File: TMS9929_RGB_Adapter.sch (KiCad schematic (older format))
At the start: 59 parts, among them P1 CONN_01X06, P10 12V, P2 CONN_01X08, P3 SEL, P4 SEL, P5 SEL, P6 CONN_01X01, P7 CONN_01X01, P8 CONN_01X01, P9 CONN_01X01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

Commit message: Initial changes to new version, copyright, DRC, etc.
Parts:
- U6: symbol TL071 -> TL071-RESCUE-TMS9929_RGB_Adapter
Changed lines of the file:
@@
 EESchema Schematic File Version 2
+LIBS:TMS9929_RGB_Adapter-rescue
 LIBS:power
 LIBS:device
@@
 Sheet 1 1
 Title "TMS9929A to RGB"
-Date "2016-06-20"
+Date "2017-09-17"
 Rev "0"
-Comp "Alexis Kotlowy"
-Comment1 ""
+Comp "Gerhard Wiesinger"
+Comment1 "Based on Alexis Kotlowy"
 Comment2 ""
 Comment3 ""
@@
 U
 $Comp
-L TL071 U6
+L TL071-RESCUE-TMS9929_RGB_Adapter U6
 U 1 1 57686080
 P 10650 4850

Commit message: Updated schematic & PCB for added Cinch connectors as well as power supply connector and damping resistors/jumpers
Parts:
- added JDC1: Jack-DC, jack_2mm:jack_2mm, symbol Jack-DC
- added JUIN1, JUOUT1: Conn_01x02, rca_white, symbol Conn_01x02
- added JUSHORT1, JVSHORT1, JYINSHORT1: Conn_01x02, Pin_Header_Straight_1x02_Pitch2.54mm, symbol Conn_01x02
- added JVIN1, JVOUT1: Conn_01x02, rca_red, symbol Conn_01x02
- added JYIN1, JYOUT1: Conn_01x02, rca_black, symbol Conn_01x02
- added RUIN1, RVIN1, RYIN1: 10E, Resistors_SMD:R_0805_HandSoldering, symbol R
- added RYIN2: 10k, Resistors_SMD:R_0805_HandSoldering, symbol R
- P1: footprint Pin_Headers:Pin_Header_Straight_1x06 -> Pin_Headers:Pin_Header_Straight_1x06_Pitch2.54mm
- P2: footprint Pin_Headers:Pin_Header_Straight_1x08 -> Pin_Headers:Pin_Header_Straight_1x08_Pitch2.54mm
- P3, P4, P5: footprint Pin_Headers:Pin_Header_Straight_1x03 -> Pin_Headers:Pin_Header_Straight_1x03_Pitch2.54mm
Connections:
- net GND: now also JDC1.2, JDC1.3, JUIN1.1 (Pin_1), JUOUT1.1 (Pin_1), JVIN1.1 (Pin_1), JVOUT1.1 (Pin_1), JYIN1.1 (Pin_1), JYOUT1.1 (Pin_1)
- net U: now also JUIN1.2 (Pin_2)
- net VCC: now also JDC1.1
- net Vref: now also RYIN2.1
- net at R28.2, U2.3 (+): now also JVSHORT1.2 (Pin_2), RVIN1.2; no longer U4.3 (O/I)
- net at R29.2, U3.3 (+): now also JUSHORT1.2 (Pin_2), RUIN1.2; no longer U4.9 (O/I)
- net YIN: now reaches C6.1, P1.3 (P3)
- net YIN: now also JYIN1.2 (Pin_2), JYINSHORT1.1 (Pin_1), RYIN1.1; no longer U1.3 (+)
- net at C3.2, P2.5 (P5): now also JUOUT1.2 (Pin_2)
- net at C2.2, P2.4 (P4): now also JVOUT1.2 (Pin_2)
- net at C1.2, P2.3 (P3): now also JYOUT1.2 (Pin_2)
- net V: now reaches P1.5 (P5), U4.4 (I/O)
- net V: now also JVIN1.2 (Pin_2)
- new net: JYINSHORT1.2 (Pin_2), RYIN1.2, RYIN2.2, U1.3 (+)
- new net: JUSHORT1.1 (Pin_1), RUIN1.1, U4.9 (O/I)
- new net: JVSHORT1.1 (Pin_1), RVIN1.1, U4.3 (O/I)
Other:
- moved on the sheet: P10, R28, R29

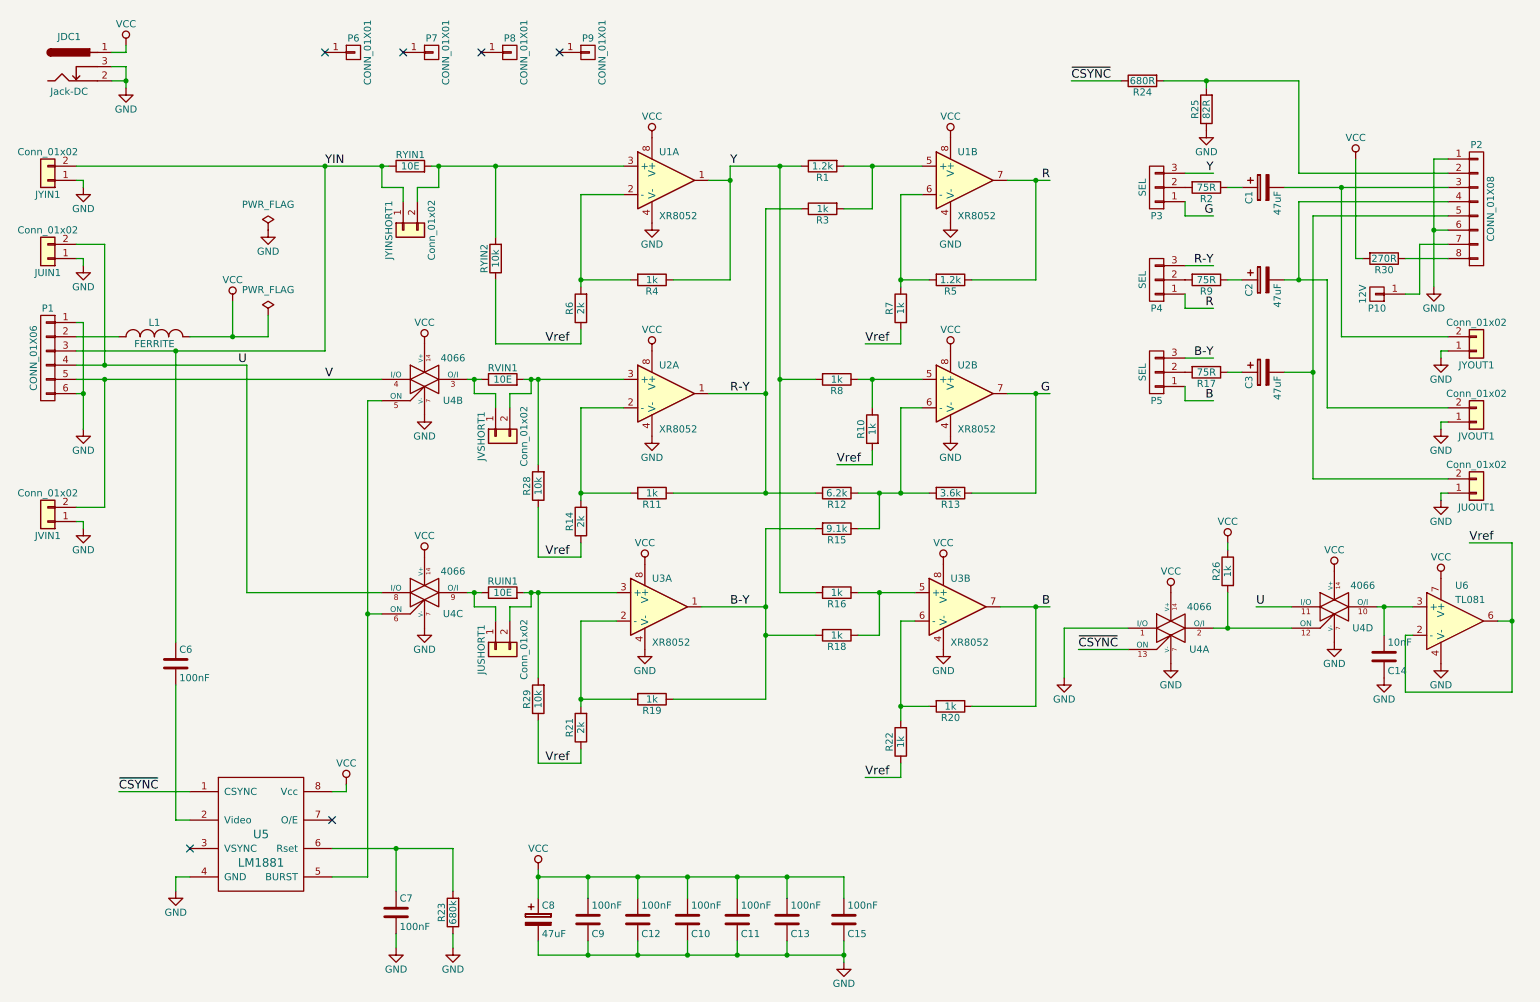
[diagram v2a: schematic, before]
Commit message: schematic: Added comments for power supply, moved capacitor at TL081 (cosmetics)
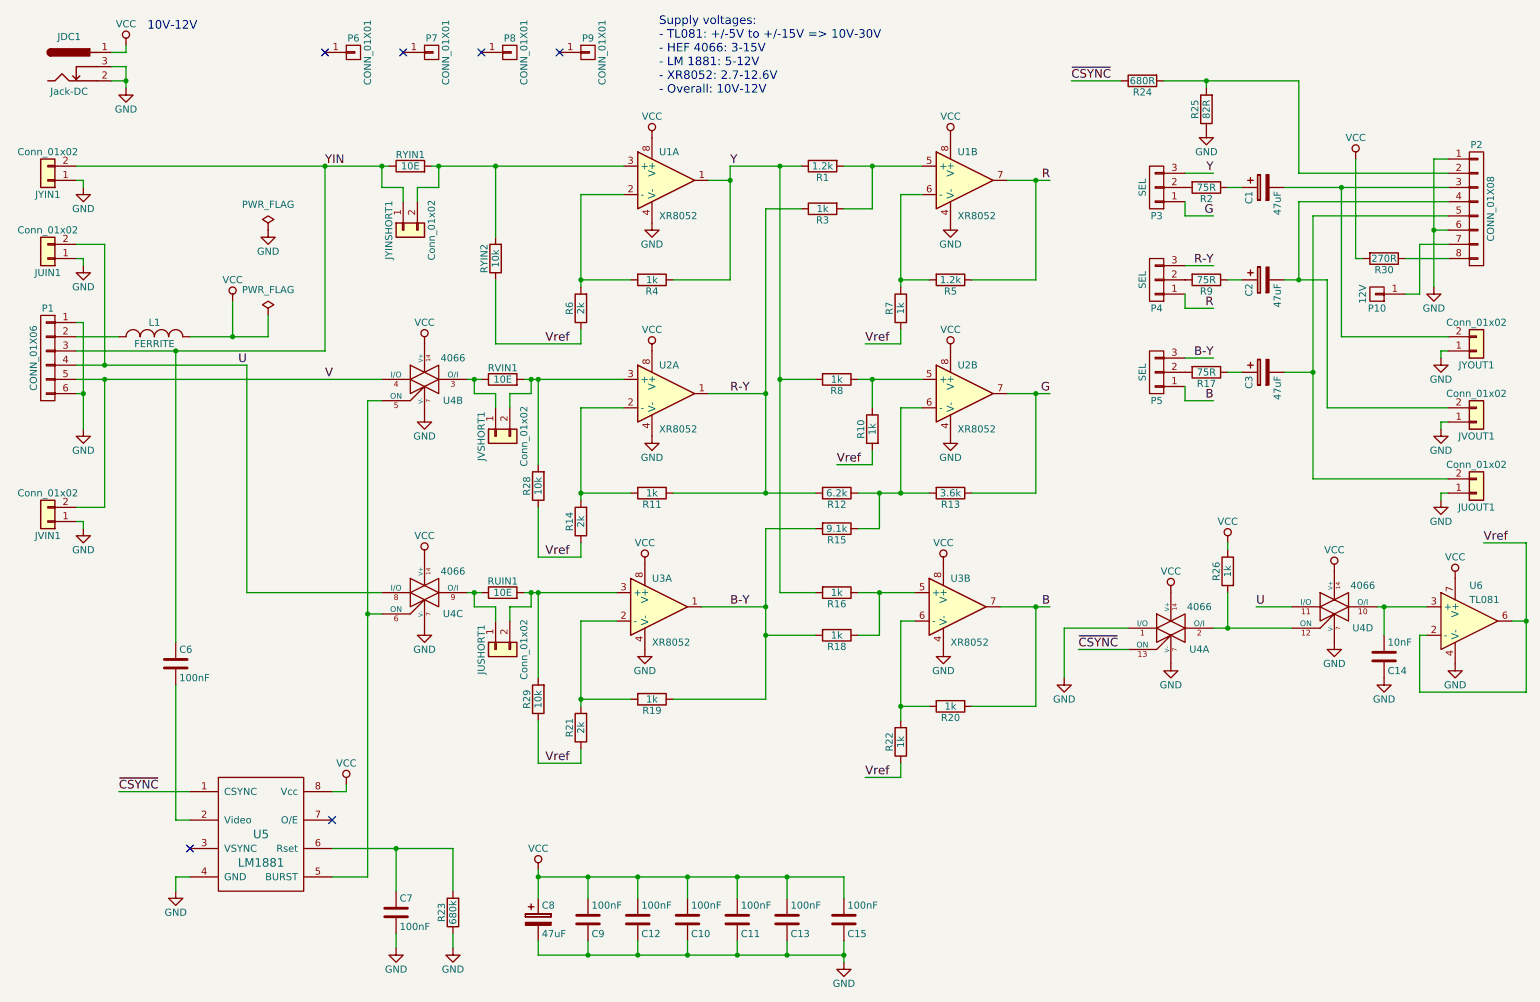
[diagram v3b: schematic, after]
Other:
- note added: "10V-12V"
- note added: "Supply voltages:\n- TL081: +/-5V to +/-15V => 10V-30V\n- HEF 4066: 3-15V\n- LM 1881: 5-12V\n- XR8052: 2.7-12.6V\n- Overall: 10V-12V\n"
- moved on the sheet: U6
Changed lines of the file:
@@
 L TL071-RESCUE-TMS9929_RGB_Adapter U6
 U 1 1 57686080
-P 10650 4850
-F 0 "U6" H 10650 5100 50  0000 L CNN
-F 1 "TL081" H 10650 5000 50  0000 L CNN
-F 2 "SMD_Packages:SOIC-8-N" H 10700 5050 50  0001 C CNN
-F 3 "" H 10650 5100 50  0000 C CNN
-	1    10650 4850
+P 10750 4850
+F 0 "U6" H 10750 5100 50  0000 L CNN
+F 1 "TL081" H 10750 5000 50  0000 L CNN
+F 2 "SMD_Packages:SOIC-8-N" H 10800 5050 50  0001 C CNN
+F 3 "" H 10750 5100 50  0000 C CNN
+	1    10750 4850
 	1    0    0    -1
 $EndComp
@@
 	1    0    0    -1
 $EndComp
-Text Label 10750 4300 0    60   ~ 0
+Text Label 10850 4300 0    60   ~ 0
 Vref
 $Comp
 L GND #PWR028
 U 1 1 57686D31
-P 10550 5150
-F 0 "#PWR028" H 10550 4900 50  0001 C CNN
-F 1 "GND" H 10550 5000 50  0000 C CNN
-F 2 "" H 10550 5150 50  0000 C CNN
-F 3 "" H 10550 5150 50  0000 C CNN
-	1    10550 5150
+P 10650 5150
+F 0 "#PWR028" H 10650 4900 50  0001 C CNN
+F 1 "GND" H 10650 5000 50  0000 C CNN
+F 2 "" H 10650 5150 50  0000 C CNN
+F 3 "" H 10650 5150 50  0000 C CNN
+	1    10650 5150
 	1    0    0    -1
 $EndComp
@@
 L VCC #PWR030
 U 1 1 576E2B1F
-P 10550 4550
-F 0 "#PWR030" H 10550 4400 50  0001 C CNN
-F 1 "VCC" H 10550 4700 50  0000 C CNN
-F 2 "" H 10550 4550 50  0000 C CNN
-F 3 "" H 10550 4550 50  0000 C CNN
-	1    10550 4550
+P 10650 4550
+F 0 "#PWR030" H 10650 4400 50  0001 C CNN
+F 1 "VCC" H 10650 4700 50  0000 C CNN
+F 2 "" H 10650 4550 50  0000 C CNN
+F 3 "" H 10650 4550 50  0000 C CNN
+	1    10650 4550
 	1    0    0    -1
 $EndComp
@@
 Wire Wire Line
 	6350 7100 6350 7250
-Connection ~ 11050 4850
-Wire Wire Line
-	11050 4300 10750 4300
+Connection ~ 11150 4850
+Wire Wire Line
+	11150 4300 10850 4300
 Connection ~ 10150 4750
 Wire Wire Line
 	10150 4950 10150 4750
 Wire Wire Line
-	11050 4850 10950 4850
-Wire Wire Line
-	11050 4300 11050 5350
-Wire Wire Line
-	11050 5350 10300 5350
-Wire Wire Line
-	10300 5350 10300 4950
-Wire Wire Line
-	10300 4950 10350 4950
-Wire Wire Line
-	10100 4750 10350 4750
+	11150 4850 11050 4850
+Wire Wire Line
+	11150 4300 11150 5350
+Wire Wire Line
+	11150 5350 10400 5350
+Wire Wire Line
+	10400 5350 10400 4950
+Wire Wire Line
+	10400 4950 10450 4950
+Wire Wire Line
+	10100 4750 10450 4750
 Wire Wire Line
 	9500 4750 9250 4750
@@
 	9850 2850 9850 1800
 Connection ~ 9850 1800
+Text Notes 1450 700  0    60   ~ 0
+10V-12V
+Text Notes 5050 1150 0    60   ~ 0
+Supply voltages:\n- TL081: +/-5V to +/-15V => 10V-30V\n- HEF 4066: 3-15V\n- LM 1881: 5-12V\n- XR8052: 2.7-12.6V\n- Overall: 10V-12V\n
 $EndSCHEMATC
